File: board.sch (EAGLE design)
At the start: 82 parts, among them IC1 REG1117F, J1 LHBEAMOUT, J10 TEMP, J11 HORNOUT, J12 12V_SUPPLY, J13 STOPOUT, J14 TURNOUT, J15 FANOUT, J16 BLIGHTOUT, J17 AUXOUT, J18 AUX, J19 CAN, J2 BATT, J3 BLIGHT, J4 LHBEAM, J5 LRTURN, J6 WARNING, J7 HORN, J9 BREAK, Q1 FQD19N10LTM, Q2 FQD19N10LTM, Q3 FQD19N10LTM, Q4 IRF7424TRPBF, Q5 IRF7424TRPBF, Q6 IRF7424TRPBF, Q7 IRF7424TRPBF, Q8 IRF7424TRPBF, Q9 IRF7424TRPBF, U1 VOM1271T, U2 VOM1271T, U3 VOM1271T, U4 MC14504BDR2G, U5 MAX3051ESA+T

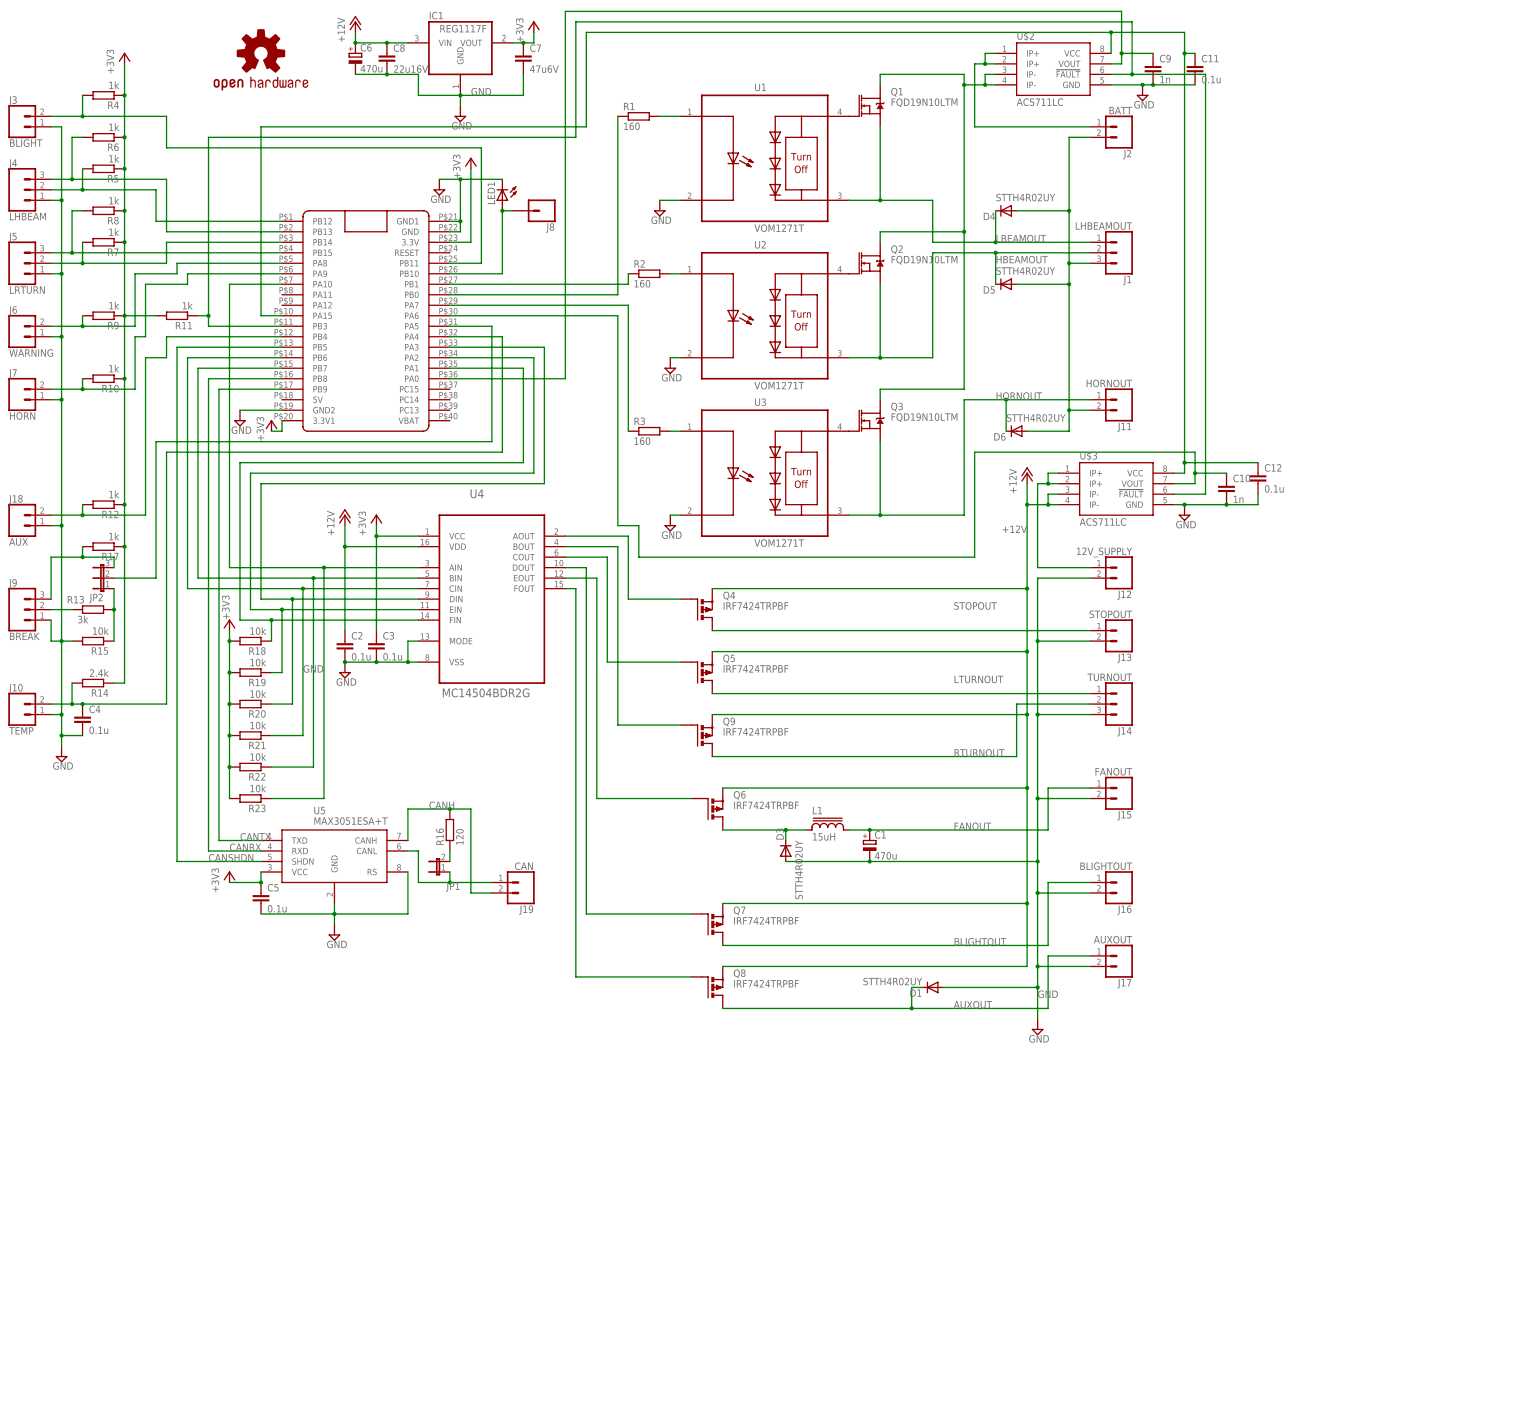
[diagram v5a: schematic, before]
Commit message: Board v2, firmware is still WIP
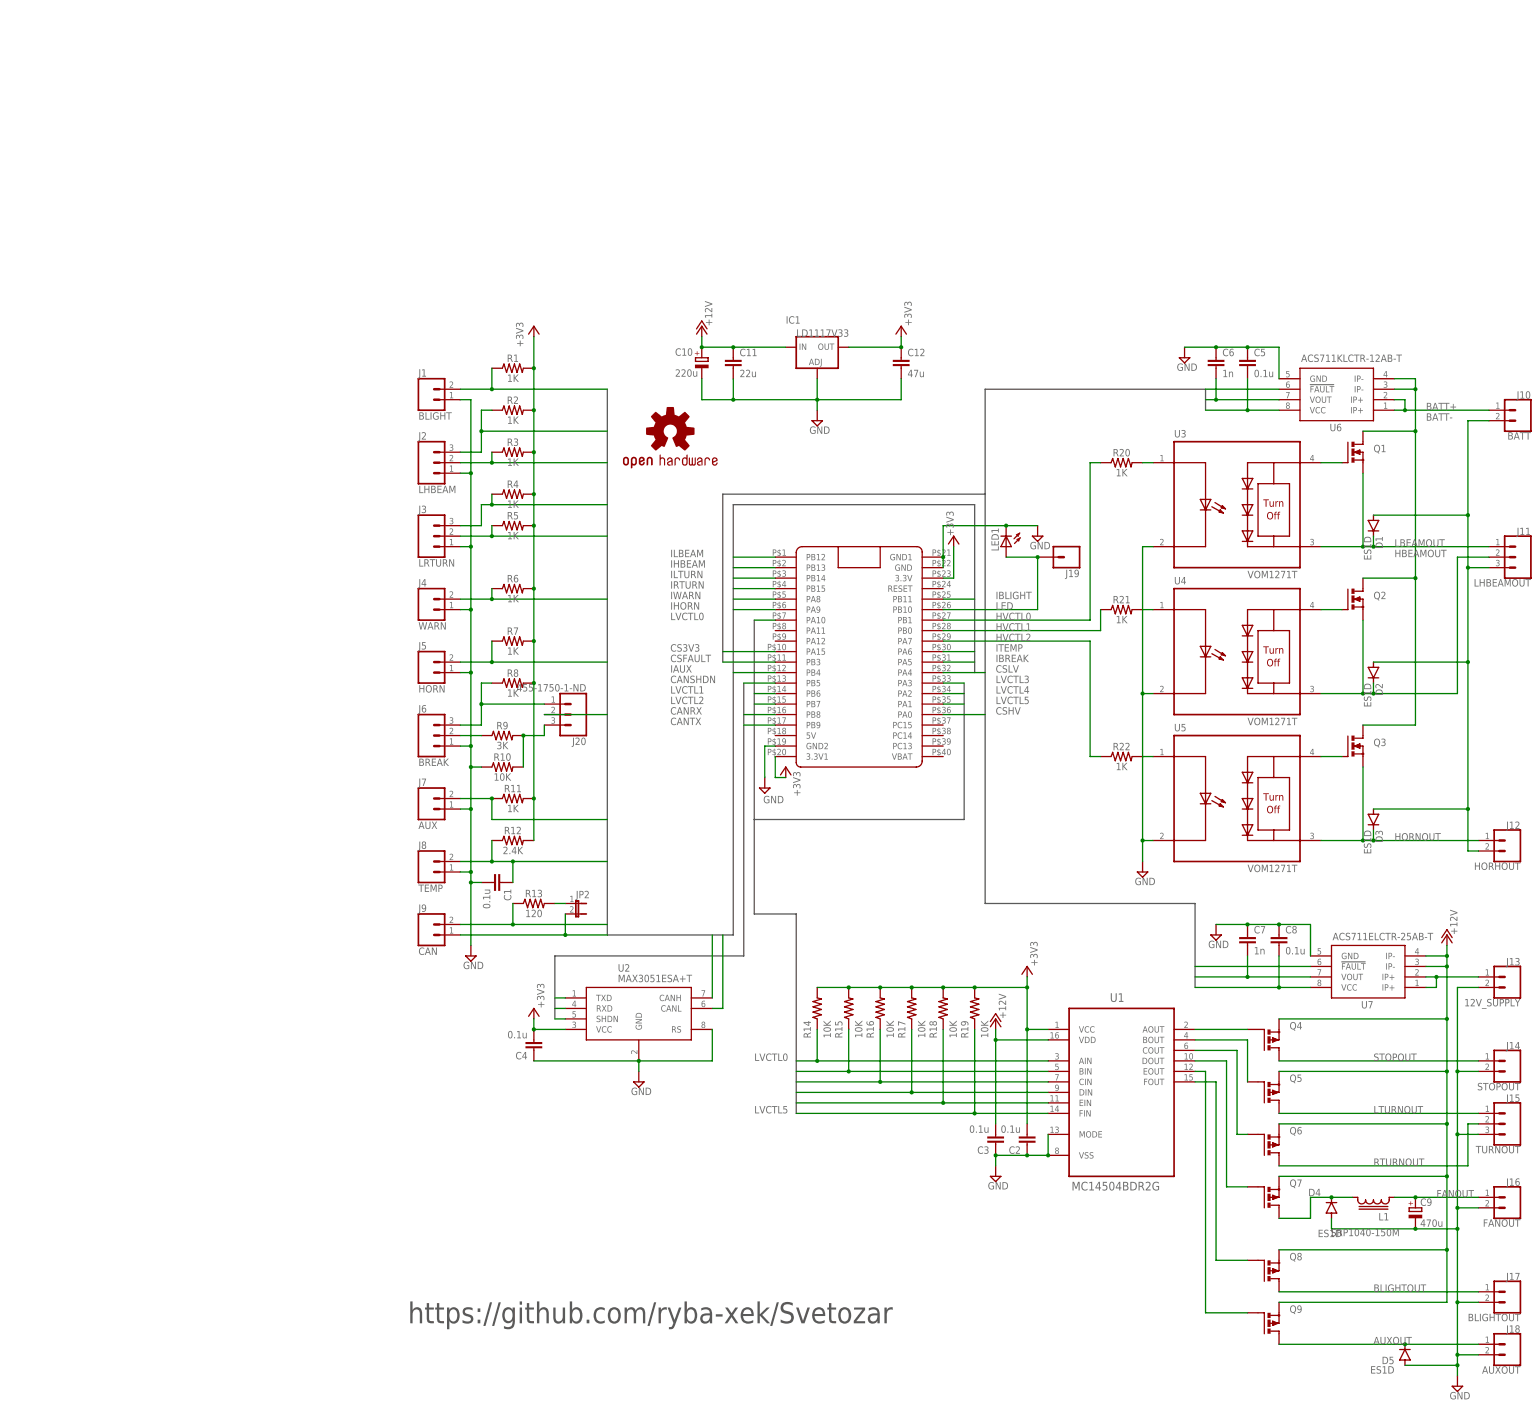
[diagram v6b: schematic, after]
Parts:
- removed D6: STTH4R02UY, diode:DIODE-SMB
- removed JP1: (no value), jumper:JP1E
- removed LOGO2: OSHW-LOGOL, SparkFun-Aesthetics:OSHW-LOGOL
- removed R23: 10k, rcl:R-EU_R0603
- removed U$2, U$3: ACS711LC, svetozar:ACS711
- added D2: ES1D, diode:DIODE-DO214AC
- added J20: 455-1750-1-ND, SparkFun-Connectors:CONN_03
- added LOGO1: OSHW-LOGOL, SparkFun-Aesthetics:OSHW-LOGOL
- added U6: ACS711KLCTR-12AB-T, svetozar:ACS711
- added U7: ACS711ELCTR-25AB-T, svetozar:ACS711
- C1: value 470u -> 0.1u; device rcl:CPOL-EUF -> rcl:C-EUC0805; MPN SK016M0470B3F-0811 -> CC0805KRX7R9BB104; PRICE 2,70р -> (none); SHOP https://www.terraelectronica.ru/product/1262453 -> (none)
- C10: value 1n -> 220u; device rcl:C-EUC0805 -> rcl:CPOL-EUE2.5-6
- C11: value 0.1u -> 22u; device rcl:C-EUC0805 -> rcl:C-EUC1206
- C12: value 0.1u -> 47u; device rcl:C-EUC0805 -> rcl:C-EUC1206
- C2: device rcl:C-EUC1206 -> rcl:C-EUC0805; MPN CC1206KRX7R8BB104 -> CC0805KRX7R9BB104; PRICE 2,20р -> (none); SHOP https://www.terraelectronica.ru/product/540763 -> (none)
- C3: device rcl:C-EUC0805 -> rcl:C-EUC1206; MPN CC0805KRX7R9BB104 -> CC1206KRX7R8BB104; PRICE 2,00р -> (none); SHOP https://www.terraelectronica.ru/product/251110 -> (none)
- C4, C5: MPN (none) -> CC0805KRX7R9BB104
- C6: value 470u -> 1n; device rcl:CPOL-EUF -> rcl:C-EUC0805; MPN SK016M0470B3F-0811 -> CL21B102KBANNNC; PRICE 2,70р -> (none); SHOP https://www.terraelectronica.ru/product/1262453 -> (none)
- C7: value 47u6V -> 1n; device rcl:C-EUC1206 -> rcl:C-EUC0805; MPN CL31A476MQHNNNE -> CL21B102KBANNNC; PRICE 7,70р -> (none); SHOP https://www.terraelectronica.ru/product/882710 -> (none)
- C8: value 22u16V -> 0.1u; device rcl:C-EUC1206 -> rcl:C-EUC0805; MPN CL31A226KOHNNNE -> CC0805KRX7R9BB104; PRICE 12,80р -> (none); SHOP https://www.terraelectronica.ru/product/1641407 -> (none)
- C9: value 1n -> 470u; device rcl:C-EUC0805 -> rcl:CPOL-EUE3.5-8
- D1, D3, D4, D5: value STTH4R02UY -> ES1D; device diode:DIODE-SMB -> diode:DIODE-DO214AC; MPN STTH4R02U -> (none); PRICE 14,10р -> (none); SHOP https://www.terraelectronica.ru/product/450947 -> (none)
- IC1: value REG1117F -> LD1117V33; device burr-brown:REG1117F -> v-reg:LD117ADT33TR; MPN LD1117S33TR -> NCP1117DT33G; PRICE 12,00р -> (none); SHOP https://www.terraelectronica.ru/product/208059 -> (none)
- J1: value LHBEAMOUT -> BLIGHT; device SparkFun-Connectors:CONN_03SCREW -> SparkFun-Connectors:CONN_023.5MM; MPN DG350-3.5-03P-14-00AH -> DG350-3.5-02P-14-00AH; PRICE 9,40р -> (none); SHOP https://www.terraelectronica.ru/product/1108750 -> (none)
- J10: value TEMP -> BATT; PRICE 5,80р -> (none); SHOP https://www.terraelectronica.ru/product/1115132 -> (none)
- J11: value HORNOUT -> LHBEAMOUT; device SparkFun-Connectors:CONN_023.5MM -> SparkFun-Connectors:CONN_03SCREW; MPN DG350-3.5-02P-14-00AH -> DG350-3.5-03P-14-00AH; PRICE 5,80р -> (none); SHOP https://www.terraelectronica.ru/product/1115132 -> (none)
- J12: value 12V_SUPPLY -> HORHOUT; PRICE 5,80р -> (none); SHOP https://www.terraelectronica.ru/product/1115132 -> (none)
- J13: value STOPOUT -> 12V_SUPPLY; PRICE 5,80р -> (none); SHOP https://www.terraelectronica.ru/product/1115132 -> (none)
- J14: value TURNOUT -> STOPOUT; device SparkFun-Connectors:CONN_03SCREW -> SparkFun-Connectors:CONN_023.5MM; MPN DG350-3.5-03P-14-00AH -> DG350-3.5-02P-14-00AH; PRICE 9,40р -> (none); SHOP https://www.terraelectronica.ru/product/1108750 -> (none)
- J15: value FANOUT -> TURNOUT; device SparkFun-Connectors:CONN_023.5MM -> SparkFun-Connectors:CONN_03SCREW; MPN DG350-3.5-02P-14-00AH -> DG350-3.5-03P-14-00AH; PRICE 5,80р -> (none); SHOP https://www.terraelectronica.ru/product/1115132 -> (none)
- J16: value BLIGHTOUT -> FANOUT; PRICE 5,80р -> (none); SHOP https://www.terraelectronica.ru/product/1115132 -> (none)
- J17: value AUXOUT -> BLIGHTOUT; PRICE 5,80р -> (none); SHOP https://www.terraelectronica.ru/product/1115132 -> (none)
- J18: value AUX -> AUXOUT; PRICE 5,80р -> (none); SHOP https://www.terraelectronica.ru/product/1115132 -> (none)
- J19: value CAN -> (none); device SparkFun-Connectors:CONN_023.5MM -> SparkFun-Connectors:CONN_01; MPN DG350-3.5-02P-14-00AH -> (none); PRICE 5,80р -> (none); SHOP https://www.terraelectronica.ru/product/1115132 -> (none)
- J2: value BATT -> LHBEAM; device SparkFun-Connectors:CONN_023.5MM -> SparkFun-Connectors:CONN_03SCREW; MPN DG350-3.5-02P-14-00AH -> DG350-3.5-03P-14-00AH; PRICE 5,80р -> (none); SHOP https://www.terraelectronica.ru/product/1115132 -> (none)
- J3: value BLIGHT -> LRTURN; device SparkFun-Connectors:CONN_023.5MM -> SparkFun-Connectors:CONN_03SCREW; MPN DG350-3.5-02P-14-00AH -> DG350-3.5-03P-14-00AH; PRICE 5,80р -> (none); SHOP https://www.terraelectronica.ru/product/1115132 -> (none)
- J4: value LHBEAM -> WARN; device SparkFun-Connectors:CONN_03SCREW -> SparkFun-Connectors:CONN_023.5MM; MPN DG350-3.5-03P-14-00AH -> DG350-3.5-02P-14-00AH; PRICE 9,40р -> (none); SHOP https://www.terraelectronica.ru/product/1108750 -> (none)
- J5: value LRTURN -> HORN; device SparkFun-Connectors:CONN_03SCREW -> SparkFun-Connectors:CONN_023.5MM; MPN DG350-3.5-03P-14-00AH -> DG350-3.5-02P-14-00AH; PRICE 9,40р -> (none); SHOP https://www.terraelectronica.ru/product/1108750 -> (none)
- J6: value WARNING -> BREAK; device SparkFun-Connectors:CONN_023.5MM -> SparkFun-Connectors:CONN_03SCREW; MPN DG350-3.5-02P-14-00AH -> DG350-3.5-03P-14-00AH; PRICE 5,80р -> (none); SHOP https://www.terraelectronica.ru/product/1115132 -> (none)
- J7: value HORN -> AUX; PRICE 5,80р -> (none); SHOP https://www.terraelectronica.ru/product/1115132 -> (none)
- J8: value (none) -> TEMP; device SparkFun-Connectors:CONN_01 -> SparkFun-Connectors:CONN_023.5MM; MPN (none) -> DG350-3.5-02P-14-00AH
- J9: value BREAK -> CAN; device SparkFun-Connectors:CONN_03SCREW -> SparkFun-Connectors:CONN_023.5MM; PRICE 5,80р -> (none); SHOP https://www.terraelectronica.ru/product/1115132 -> (none)
- JP2: device jumper:JP2E -> jumper:JP1E
- L1: value 15uH -> SRP1040-150M; device inductor-bourns:SDR1307 -> inductor-bourns:SRP1040; MPN SDR1307-150ML -> SRP1040-150M; PRICE 21,20р -> (none); SHOP https://www.terraelectronica.ru/product/607745 -> (none)
- Q1, Q2, Q3: value FQD19N10LTM -> PHP20NQ20T; device SparkFun-DiscreteSemi:MOSFET-NCH-FDD8780 -> transistor-power:PMOSFET_NTO220BV; MPN FQD19N10LTM -> (none); PRICE 15,80р -> (none); SHOP https://www.terraelectronica.ru/product/675613 -> (none)
- Q4, Q5, Q9: value IRF7424TRPBF -> (none); MPN IRLML9301TRPBF -> (none); PRICE 9,10р -> (none); SHOP https://www.terraelectronica.ru/product/575910 -> (none)
- Q6, Q7, Q8: value IRF7424TRPBF -> (none); MPN IRF7424TRPBF -> (none); PRICE 15,40р -> (none); SHOP https://www.terraelectronica.ru/product/301875 -> (none)
- R1: value 160 -> 1K; device rcl:R-EU_R0805 -> SparkFun-Resistors:RESISTOR0603; MPN RC0805FR-07160RL -> (none); PRICE 0,52р -> (none); SHOP https://www.terraelectronica.ru/product/880371 -> (none)
- R10, R17: value 1k -> 10K; device rcl:R-EU_R0603 -> SparkFun-Resistors:RESISTOR0603
- R11: value 1k -> 1K; device rcl:R-EU_R0805 -> SparkFun-Resistors:RESISTOR0603
- R12: value 1k -> 2.4K; device rcl:R-EU_R0603 -> SparkFun-Resistors:RESISTOR0603
- R13: value 3k -> 120; device rcl:R-EU_R0603 -> SparkFun-Resistors:RESISTOR0603; MPN RC0805JR-071KL -> (none); PRICE 0,17р -> (none); SHOP https://www.terraelectronica.ru/product/443003 -> (none)
- R14: value 2.4k -> 10K; device rcl:R-EU_R0603 -> SparkFun-Resistors:RESISTOR0603; MPN RC0805FR-072K4L -> (none); PRICE 0,15р -> (none); SHOP https://www.terraelectronica.ru/product/562267 -> (none)
- R15, R18, R19: value 10k -> 10K; device rcl:R-EU_R0603 -> SparkFun-Resistors:RESISTOR0603; MPN RC0805JR-0710KL -> (none); PRICE 0,24р -> (none); SHOP https://www.terraelectronica.ru/product/339147 -> (none)
- R16: value 120 -> 10K; device rcl:R-EU_R0805 -> SparkFun-Resistors:RESISTOR0603; MPN RC0805FR-07120RL -> (none); PRICE 0,23р -> (none); SHOP https://www.terraelectronica.ru/product/542987 -> (none)
- R2, R3: value 160 -> 1K; device rcl:R-EU_R0805 -> SparkFun-Resistors:RESISTOR0603; MPN RC0805FR-07160RL -> (none)
- R20, R21, R22: value 10k -> 1K; device rcl:R-EU_R0603 -> SparkFun-Resistors:RESISTOR0603; MPN RC0805JR-0710KL -> (none); PRICE 0,24р -> (none); SHOP https://www.terraelectronica.ru/product/339147 -> (none)
- R4: value 1k -> 1K; device rcl:R-EU_R0603 -> SparkFun-Resistors:RESISTOR0603; MPN RC0805JR-071KL -> (none); PRICE 0,19р -> (none); SHOP https://www.terraelectronica.ru/product/559515 -> (none)
- R5, R6, R7, R8: value 1k -> 1K; device rcl:R-EU_R0603 -> SparkFun-Resistors:RESISTOR0603
- R9: value 1k -> 3K; device rcl:R-EU_R0603 -> SparkFun-Resistors:RESISTOR0603
- U$1: device BluePill:BLUE_PILL -> svetozar:BLUE_PILL; MPN Blue Pill -> (none); PRICE 127,73р -> (none); SHOP https://ru.aliexpress.com/item/STM32F103C8T6-ARM-STM32-Mini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 -> (none)
- U1: value VOM1271T -> MC14504BDR2G; device VOM1271T:VOM1271T -> MC14504BDR2G:MC14504BDR2G; MPN VOM1271T -> (none); PRICE 173,00р -> (none); SHOP https://www.terraelectronica.ru/product/1112827 -> (none)
- U2: value VOM1271T -> MAX3051ESA+T; device VOM1271T:VOM1271T -> MAX3051ESA:MAX3051ESA+T; MPN VOM1271T -> (none); PRICE 173,00р -> (none); SHOP https://www.terraelectronica.ru/product/1112827 -> (none)
- U3: MPN VOM1271T -> (none); PRICE 173,00р -> (none); SHOP https://www.terraelectronica.ru/product/1112827 -> (none)
- U4: value MC14504BDR2G -> VOM1271T; device MC14504BDR2G:MC14504BDR2G -> VOM1271T:VOM1271T; MPN MC14504BDR2G -> (none); PRICE 25,70р -> (none); SHOP https://www.terraelectronica.ru/product/284776 -> (none)
- U5: value MAX3051ESA+T -> VOM1271T; device MAX3051ESA:MAX3051ESA+T -> VOM1271T:VOM1271T; MPN MAX3051ESA+T -> (none); PRICE 141,00р -> (none); SHOP https://www.terraelectronica.ru/product/462120 -> (none)
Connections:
- removed net ABRK_S: JP2.2, U$1.PA5
- removed net BATT+IN: J2.1, U$2.IP+@1, U$2.IP+@2
- removed net CSENS1: C9.1, U$1.PA0, U$2.VOUT
- removed net FAULT: R11.1, U$1.PB3, U$2.!FAULT, U$3.!FAULT
- removed net HV1CTL: R1.1, U$1.PB0
- removed net HV1CTLG: R1.2, U1.A1
- removed net HV1G: Q1.G, U1.A2
- removed net HV2CTL: R2.1, U$1.PB1
- removed net HV2CTLG: R2.2, U2.A1
- removed net HV2G: Q2.G, U2.A2
- removed net HV3CTL: R3.1, U$1.PA7
- removed net HV3CTLG: R3.2, U3.A1
- removed net HV3G: Q3.G, U3.A2
- removed net IATEMP: C4.1, J10.2, R14.2, U$1.PA4
- removed net IBLGHT: J3.2, R4.2, U$1.PB11
- removed net LV1G: Q8.G, U4.FOUT
- removed net LV2G: Q7.G, U4.DOUT
- removed net LV3G: Q6.G, U4.EOUT
- removed net LV4G: Q4.G, U4.AOUT
- removed net LV5G: Q9.G, U4.BOUT
- removed net LV6G: Q5.G, U4.COUT
- removed net LVCTL6: R18.1, U$1.PA1, U4.FIN
- removed net N$17: D3.C, L1.1, Q6.D
- removed net N$29: J4.3, R6.2, U$1.PB13
- removed net N$30: J4.2, R5.2, U$1.PB12
- removed net N$31: J7.2, R10.2, U$1.PA9
- removed net N$32: J5.3, R8.2, U$1.PB15
- removed net N$33: J5.2, R7.2, U$1.PB14
- removed net N$35: J6.2, R9.2, U$1.PA8
- removed net N$5: J9.2, R13.1
- removed net N$6: J8.1, LED1.A, U$1.PB10
- removed net N$7: J12.1, U$3.IP+@1, U$3.IP+@2
- removed net N$8: C10.1, U$1.PA6, U$3.VOUT
- new net 12V_IN: J13.1, U7.IP+@1, U7.IP+@2
- new net CANL: J9.2, R13.1, U2.CANL
- new net CS3V3: C5.2, C8.2, U$1.PA15, U6.VCC, U7.VCC
- new net CSFAULT: U$1.PB3, U6.!FAULT, U7.!FAULT
- new net CSHV: C6.2, U$1.PA0, U6.VOUT
- new net CSLV: C7.2, U$1.PA4, U7.VOUT
- new net FANPWM: D4.C, L1.2, Q7.D
- new net HV: Q1.D, Q2.D, Q3.D, U6.IP-@3, U6.IP-@4
- new net HVCTL0: R20.1, U$1.PB1
- new net HVCTL1: R21.1, U$1.PB0
- new net HVCTL2: R22.1, U$1.PA7
- new net IBLIGHT: J1.2, R1.1, U$1.PB11
- new net IBREAK: J20.2, U$1.PA5
- new net IHBEAM: J2.2, R3.1, U$1.PB13
- new net IHORN: J5.2, R7.1, U$1.PA9
- new net ILBEAM: J2.3, R2.1, U$1.PB12
- new net ILTURN: J3.3, R4.1, U$1.PB14
- new net IRTURN: J3.2, R5.1, U$1.PB15
- new net ITEMP: C1.1, J8.2, R12.1, U$1.PA6
- new net IWARN: J4.2, R6.1, U$1.PA8
- new net LED: J19.1, LED1.A, U$1.PB10
- new net LVCTL0: R14.1, U$1.PA10, U1.AIN
- new net LVG0: Q4.G, U1.AOUT
- new net LVG1: Q5.G, U1.BOUT
- new net LVG2: Q6.G, U1.COUT
- new net LVG3: Q7.G, U1.DOUT
- new net LVG4: Q8.G, U1.FOUT
- new net LVG5: Q9.G, U1.EOUT
- new net N$10: Q1.G, U3.A2
- new net N$11: R21.2, U4.A1
- new net N$12: Q2.G, U4.A2
- new net N$13: R22.2, U5.A1
- new net N$14: Q3.G, U5.A2
- net +12V: now also C10.+, C11.1, C3.2, IC1.IN, U1.VDD, U7.IP-@3, U7.IP-@4; no longer C2.1, C6.+, C8.1, IC1.VIN, U$3.IP-@3, U$3.IP-@4, U4.VDD
- net +3V3: now also C12.1, C2.2, C4.2, IC1.OUT, R1.2, R12.2, R14.2, R15.2, R16.2, R17.2, R2.2, R3.2, R4.2, R5.2, R6.2, R7.2, R8.2, U1.VCC, U2.VCC; no longer C3.1, C5.1, C7.1, IC1.VOUT, R10.1, R12.1, R14.1, R17.1, R20.2, R21.2, R22.2, R23.2, R4.1, R5.1, R6.1, R7.1, R8.1, R9.1, U4.VCC, U5.VCC
- net AUXOUT: now also D5.C, J18.1, Q9.D; no longer D1.C, J17.1, Q8.D
- net BATT+: now also J10.1, U6.IP+@1, U6.IP+@2; no longer Q1.D, Q2.D, Q3.D, U$2.IP-@3, U$2.IP-@4
- net BATT-: now also D1.A, D2.A, D3.A, J10.2, J11.3, J12.2; no longer D4.A, D5.A, D6.A, J1.3, J11.2, J2.2
- net BLIGHTOUT: now also J17.1, Q8.D; no longer J16.1, Q7.D
- net CANH: now also J9.1, JP2.2, U2.CANH; no longer J19.2, R16.2, U5.CANH
- net CANRX: now also U2.RXD; no longer U5.RXD
- net CANSHDN: now also U2.SHDN; no longer U5.SHDN
- net CANTX: now also U2.TXD; no longer U5.TXD
- net FANOUT: now also C9.+, J16.1, L1.1; no longer C1.+, J15.1, L1.2
- net GND: now also C1.2, C10.-, C2.1, C3.1, C4.1, C5.1, C6.1, C7.1, C8.1, C9.-, D4.A, D5.A, IC1.ADJ, J1.1, J14.2, J15.3, J18.2, J2.1, J8.1, R10.1, U1.MODE, U1.VSS, U2.GND, U2.RS, U4.C1, U5.C1, U6.GND, U7.GND; no longer C1.-, C10.2, C2.2, C3.2, C4.2, C5.2, C6.-, C7.2, C8.2, C9.2, D1.A, D3.A, IC1.GND, J10.1, J12.2, J14.3, J15.2, J18.1, J9.1, R15.2, U$2.GND, U$3.GND, U1.C1, U2.C1, U4.MODE, U4.VSS, U5.GND, U5.RS
- net HBEAMOUT: now also D2.C, J11.2, U4.C2; no longer D5.C, J1.2, U2.C2
- net HORNOUT: now also D3.C, J12.1, U5.C2; no longer D6.C, J11.1, U3.C2
- net IAUX: now also J7.2, R11.1; no longer J18.2, R12.2
- net LBEAMOUT: now also D1.C, J11.1, U3.C2; no longer D4.C, J1.1, U1.C2
- net LTURNOUT: now also J15.1; no longer J14.1
- net LVCTL1: now also R15.1, U$1.PB6, U1.BIN; no longer R23.1, U$1.PA10, U4.AIN
- net LVCTL2: now also R16.1, U1.CIN; no longer R22.1, U4.BIN
- net LVCTL3: now also R17.1, U$1.PA3, U1.DIN; no longer R21.1, U$1.PB6, U4.CIN
- net LVCTL4: now also R18.1, U$1.PA2, U1.EIN; no longer R20.1, U$1.PA3, U4.DIN
- net LVCTL5: now also U$1.PA1, U1.FIN; no longer U$1.PA2, U4.EIN
- net N$1: now also J20.1, J6.3, R8.1; no longer JP1.2, R16.1
- net N$2: now also JP2.1, R13.2; no longer J19.1, JP1.1, U5.CANL
- net N$3: now also J20.3, R10.2, R9.2; no longer JP2.1, R13.2, R15.1
- net N$4: now also J6.2, R9.1; no longer J9.3, JP2.3, R17.2
- net N$9: now also R20.2, U3.A1; no longer C11.1, C12.1, U$1.PA15, U$2.VCC, U$3.VCC
- net RTURNOUT: now also J15.2, Q6.D; no longer J14.2, Q9.D
- net STOPOUT: now also J14.1; no longer J13.1
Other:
- note added: "https://github.com/ryba-xek/Svetozar"
- moved on the sheet: C11, C12, C2, C3, C4, C5, C7, C8, J10, J12, J13, J16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

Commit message: Updated README
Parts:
- D1, D2, D3, D4, D5: MPN (none) -> ES1D
- Q1, Q2, Q3: MPN (none) -> PHP20NQ20T.127
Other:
- note added: "Temp input is for KTY84/130 sensor, change R12 for others."
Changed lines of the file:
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@@
 <part name="R22" library="SparkFun-Resistors" deviceset="RESISTOR" device="0603" value="1K"/>
 <part name="SUPPLY4" library="supply2" library_urn="urn:adsk.eagle:library:372" deviceset="GND" device=""/>
-<part name="Q1" library="transistor-power" library_urn="urn:adsk.eagle:library:400" deviceset="PMOSFET_N" device="TO220BV" package3d_urn="urn:adsk.eagle:package:29484/3" value="PHP20NQ20T"/>
-<part name="Q2" library="transistor-power" library_urn="urn:adsk.eagle:library:400" deviceset="PMOSFET_N" device="TO220BV" package3d_urn="urn:adsk.eagle:package:29484/3" value="PHP20NQ20T"/>
-<part name="Q3" library="transistor-power" library_urn="urn:adsk.eagle:library:400" deviceset="PMOSFET_N" device="TO220BV" package3d_urn="urn:adsk.eagle:package:29484/3" value="PHP20NQ20T"/>
-<part name="D1" library="diode" library_urn="urn:adsk.eagle:library:210" deviceset="DIODE-" device="DO214AC" package3d_urn="urn:adsk.eagle:package:43417/2" value="ES1D"/>
-<part name="D2" library="diode" library_urn="urn:adsk.eagle:library:210" deviceset="DIODE-" device="DO214AC" package3d_urn="urn:adsk.eagle:package:43417/2" value="ES1D"/>
-<part name="D3" library="diode" library_urn="urn:adsk.eagle:library:210" deviceset="DIODE-" device="DO214AC" package3d_urn="urn:adsk.eagle:package:43417/2" value="ES1D"/>
+<part name="Q1" library="transistor-power" library_urn="urn:adsk.eagle:library:400" deviceset="PMOSFET_N" device="TO220BV" package3d_urn="urn:adsk.eagle:package:29484/3" value="PHP20NQ20T">
+<attribute name="MPN" value="PHP20NQ20T.127"/>
+</part>
+<part name="Q2" library="transistor-power" library_urn="urn:adsk.eagle:library:400" deviceset="PMOSFET_N" device="TO220BV" package3d_urn="urn:adsk.eagle:package:29484/3" value="PHP20NQ20T">
+<attribute name="MPN" value="PHP20NQ20T.127"/>
+</part>
+<part name="Q3" library="transistor-power" library_urn="urn:adsk.eagle:library:400" deviceset="PMOSFET_N" device="TO220BV" package3d_urn="urn:adsk.eagle:package:29484/3" value="PHP20NQ20T">
+<attribute name="MPN" value="PHP20NQ20T.127"/>
+</part>
+<part name="D1" library="diode" library_urn="urn:adsk.eagle:library:210" deviceset="DIODE-" device="DO214AC" package3d_urn="urn:adsk.eagle:package:43417/2" value="ES1D">
+<attribute name="MPN" value="ES1D"/>
+</part>
+<part name="D2" library="diode" library_urn="urn:adsk.eagle:library:210" deviceset="DIODE-" device="DO214AC" package3d_urn="urn:adsk.eagle:package:43417/2" value="ES1D">
+<attribute name="MPN" value="ES1D"/>
+</part>
+<part name="D3" library="diode" library_urn="urn:adsk.eagle:library:210" deviceset="DIODE-" device="DO214AC" package3d_urn="urn:adsk.eagle:package:43417/2" value="ES1D">
+<attribute name="MPN" value="ES1D"/>
+</part>
 <part name="C5" library="rcl" library_urn="urn:adsk.eagle:library:334" deviceset="C-EU" device="C0805" package3d_urn="urn:adsk.eagle:package:23617/2" value="0.1u">
 <spice>
@@
 <attribute name="MPN" value="SRP1040-150M"/>
 </part>
-<part name="D4" library="diode" library_urn="urn:adsk.eagle:library:210" deviceset="DIODE-" device="DO214AC" package3d_urn="urn:adsk.eagle:package:43417/2" value="ES1D"/>
-<part name="D5" library="diode" library_urn="urn:adsk.eagle:library:210" deviceset="DIODE-" device="DO214AC" package3d_urn="urn:adsk.eagle:package:43417/2" value="ES1D"/>
+<part name="D4" library="diode" library_urn="urn:adsk.eagle:library:210" deviceset="DIODE-" device="DO214AC" package3d_urn="urn:adsk.eagle:package:43417/2" value="ES1D">
+<attribute name="MPN" value="ES1D"/>
+</part>
+<part name="D5" library="diode" library_urn="urn:adsk.eagle:library:210" deviceset="DIODE-" device="DO214AC" package3d_urn="urn:adsk.eagle:package:43417/2" value="ES1D">
+<attribute name="MPN" value="ES1D"/>
+</part>
 <part name="IC1" library="v-reg" library_urn="urn:adsk.eagle:library:409" deviceset="LD117A?*" device="DT" package3d_urn="urn:adsk.eagle:package:30369/1" technology="33TR" value="LD1117V33">
 <attribute name="MPN" value="NCP1117DT33G"/>
@@
 <plain>
 <text x="-71.12" y="-134.62" size="5.08" layer="97">https://github.com/ryba-xek/Svetozar</text>
+<text x="-20.32" y="-12.446" size="1.778" layer="97" align="top-left">Temp input is for
+KTY84/130 sensor,
+change R12 for others.</text>
+<wire x1="-21.336" y1="-16.002" x2="-39.116" y2="-16.002" width="0.1524" layer="97"/>
 </plain>
 <instances>
@@
 <instance part="Q1" gate="G$1" x="157.48" y="76.2" smashed="yes">
 <attribute name="NAME" x="162.56" y="76.2" size="1.778" layer="95" font="vector"/>
+<attribute name="MPN" x="157.48" y="76.2" size="1.778" layer="96" display="off"/>
 </instance>
 <instance part="Q2" gate="G$1" x="157.48" y="40.64" smashed="yes">
 <attribute name="NAME" x="162.56" y="40.64" size="1.778" layer="95" font="vector"/>
+<attribute name="MPN" x="157.48" y="40.64" size="1.778" layer="96" display="off"/>
 </instance>
 <instance part="Q3" gate="G$1" x="157.48" y="5.08" smashed="yes">
 <attribute name="NAME" x="162.56" y="5.08" size="1.778" layer="95" font="vector"/>
+<attribute name="MPN" x="157.48" y="5.08" size="1.778" layer="96" display="off"/>
 </instance>
 <instance part="D1" gate="G$1" x="162.56" y="58.42" smashed="yes" rot="R270">
 <attribute name="NAME" x="163.0426" y="55.88" size="1.778" layer="95" rot="R270"/>
 <attribute name="VALUE" x="160.2486" y="55.88" size="1.778" layer="96" rot="R270"/>
+<attribute name="MPN" x="162.56" y="58.42" size="1.778" layer="96" display="off"/>
 </instance>
 <instance part="D2" gate="G$1" x="162.56" y="22.86" smashed="yes" rot="R270">
 <attribute name="NAME" x="163.0426" y="20.32" size="1.778" layer="95" rot="R270"/>
 <attribute name="VALUE" x="160.2486" y="20.32" size="1.778" layer="96" rot="R270"/>
+<attribute name="MPN" x="162.56" y="22.86" size="1.778" layer="96" display="off"/>
 </instance>
 <instance part="D3" gate="G$1" x="162.56" y="-12.7" smashed="yes" rot="R270">
 <attribute name="NAME" x="163.0426" y="-15.24" size="1.778" layer="95" rot="R270"/>
 <attribute name="VALUE" x="160.2486" y="-15.24" size="1.778" layer="96" rot="R270"/>
+<attribute name="MPN" x="162.56" y="-12.7" size="1.778" layer="96" display="off"/>
 </instance>
 <instance part="C5" gate="G$1" x="132.08" y="99.06" smashed="yes">
@@
 <attribute name="NAME" x="149.86" y="-102.0826" size="1.778" layer="95" rot="R180"/>
 <attribute name="VALUE" x="154.94" y="-111.9886" size="1.778" layer="96" rot="R180"/>
+<attribute name="MPN" x="152.4" y="-106.68" size="1.778" layer="96" display="off"/>
 </instance>
 <instance part="D5" gate="G$1" x="170.18" y="-142.24" smashed="yes" rot="R90">
 <attribute name="NAME" x="167.64" y="-142.7226" size="1.778" layer="95" rot="R180"/>
 <attribute name="VALUE" x="167.64" y="-145.0086" size="1.778" layer="96" rot="R180"/>
+<attribute name="MPN" x="170.18" y="-142.24" size="1.778" layer="96" display="off"/>
 </instance>
 <instance part="IC1" gate="G$1" x="27.94" y="101.6" smashed="yes">
@@
 </drawing>
 <compatibility>
+<note version="6.3" minversion="6.2.2" severity="warning">
+Since Version 6.2.2 text objects can contain more than one line,
+which will not be processed correctly with this version.
+</note>
 <note version="8.2" severity="warning">
 Since Version 8.2, EAGLE supports online libraries. The ids
